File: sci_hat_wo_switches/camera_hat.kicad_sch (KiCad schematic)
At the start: 0 parts

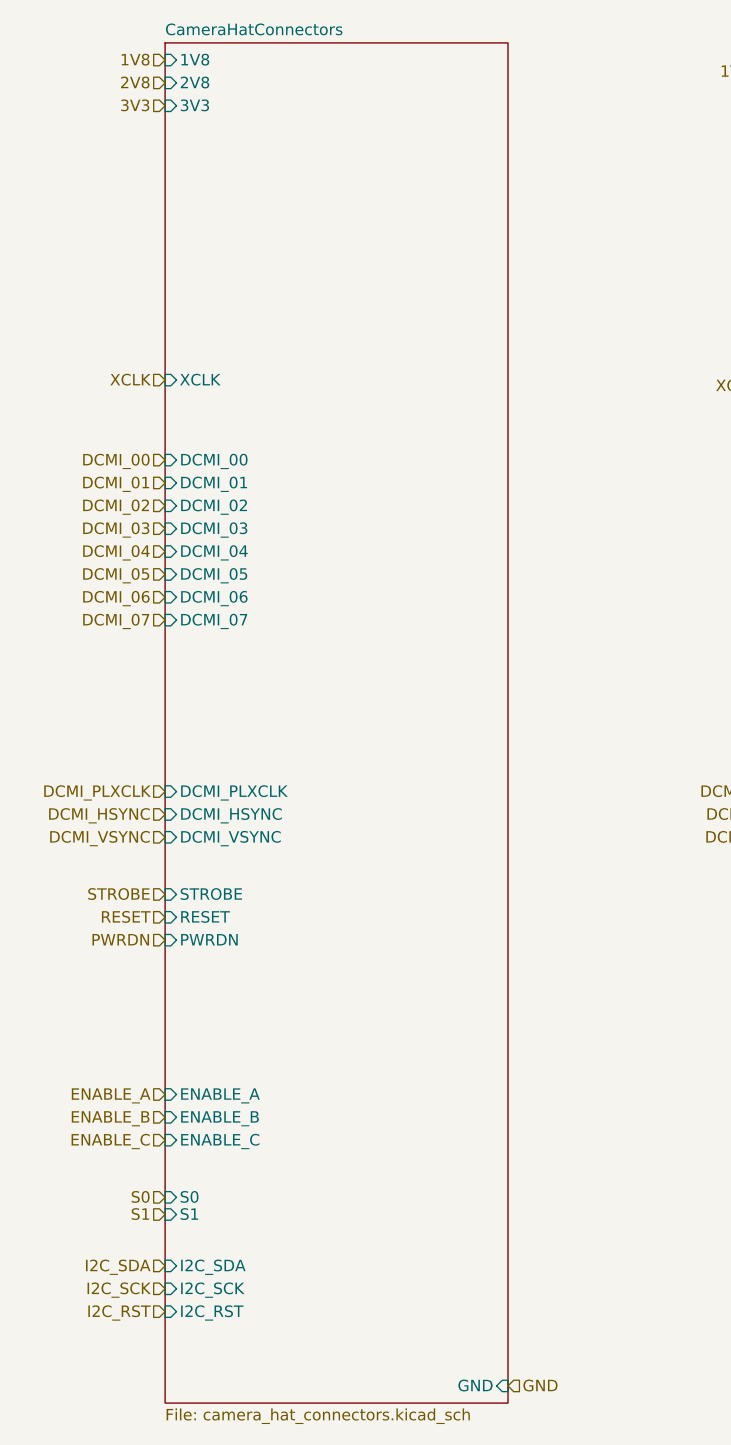
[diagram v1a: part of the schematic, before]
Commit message: move camera connector to common
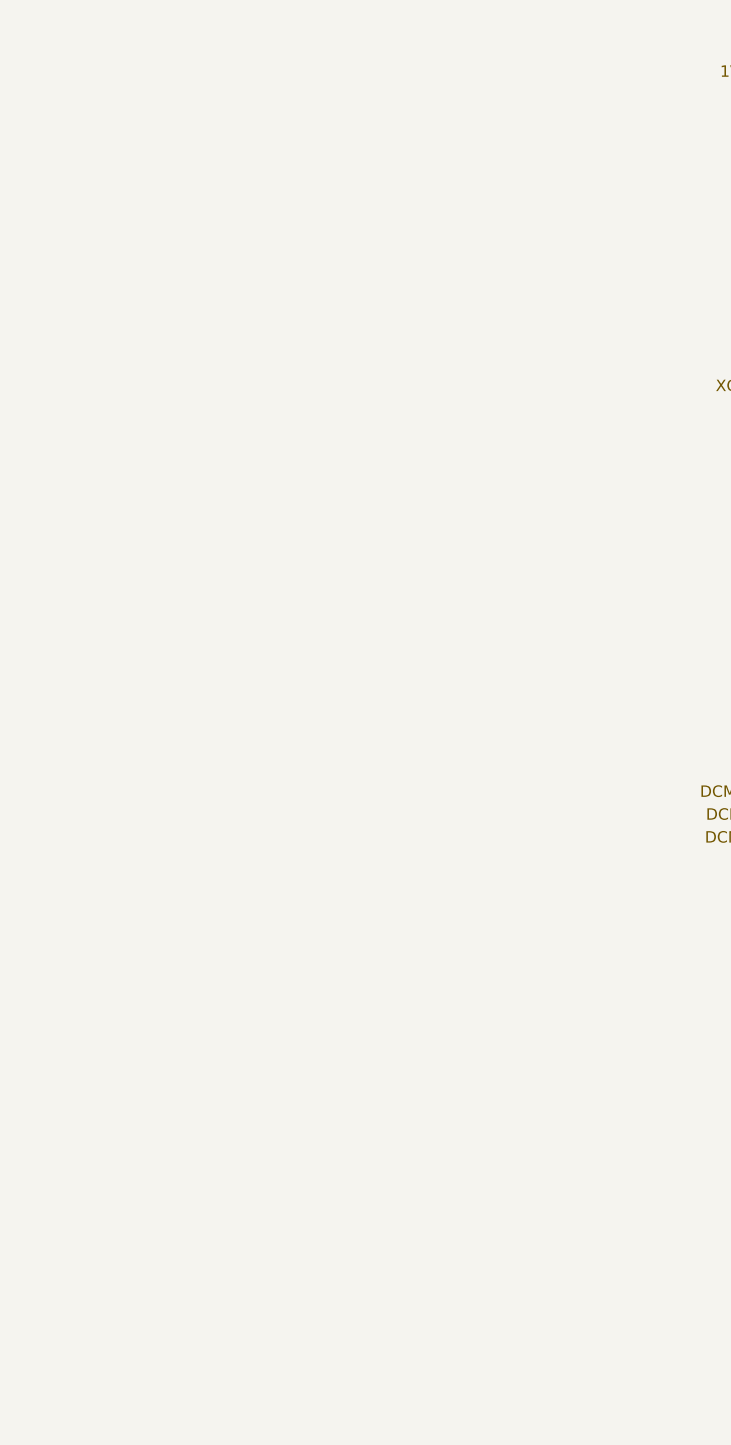
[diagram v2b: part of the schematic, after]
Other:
- removed sheet CameraHatConnectors
